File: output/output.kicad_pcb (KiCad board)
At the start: 2 copper layers, 19.1 x 108.5 mm, 60 parts, among them J1 AudioJack2_SwitchT, J2 AudioJack2_SwitchT, J3 Conn_02x05_Odd_Even, J4 AudioJack3, J5 AudioJack3, Q1 MMBT3904, Q2 MMBT3904, U1 NE5532, U2 TL074, U3 NE5532

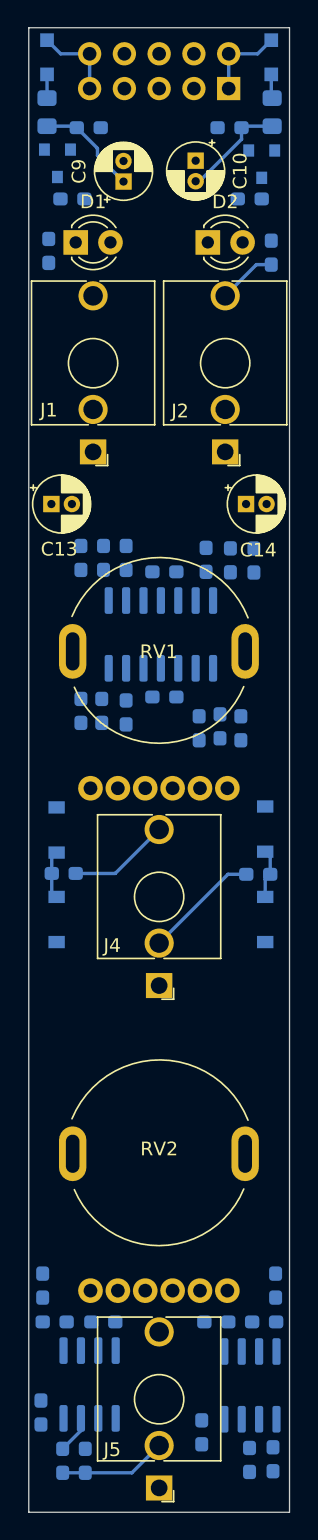
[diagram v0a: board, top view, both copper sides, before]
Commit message: Board layout for Output module
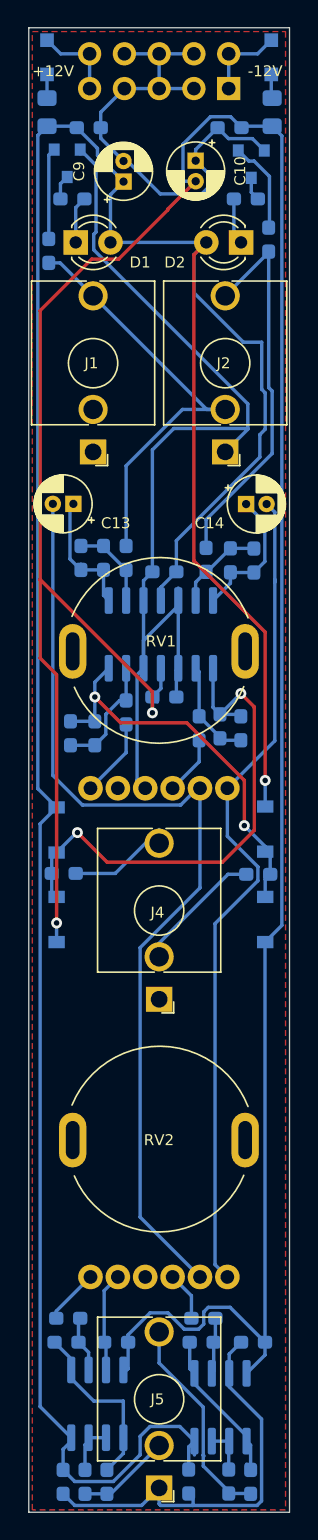
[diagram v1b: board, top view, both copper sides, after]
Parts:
- J1, J2: footprint footprints:Jack_3.5mm_QingPu_WQP-PJ398SM_Vertical_CircularHoles -> kicad_lib:Jack_3.5mm_QingPu_WQP-PJ398SM_Vertical_CircularHoles
- J4, J5: footprint footprints:Jack_3.5mm_QingPu_WQP-WQP419GR_Vertical_CircularHoles -> kicad_lib:Jack_3.5mm_QingPu_WQP-WQP419GR_Vertical_CircularHoles
- RV1, RV2: footprint footprints:Potentiometer_Song_Huei_R1214G_Dual_Vertical -> kicad_lib:Potentiometer_Song_Huei_R1214G_Dual_Vertical
- moved R9 5.79 mm to (202.8, 131.8), turned to 180 degrees
- moved C3 5.32 mm to (192.5, 143.7), turned to 270 degrees
- moved C1 3.72 mm to (201.7, 143.7)
- moved R10 3.03 mm to (192.9, 131.8), turned to 180 degrees
- moved C16 2.81 mm to (193.0, 89.0)
- moved U1 2.71 mm to (204.0, 138.2)
- moved D2 2.43 mm to (205.5, 53.1), turned to 180 degrees
- moved R20 2.32 mm to (206.2, 143.7)
- moved R21 2.24 mm to (194.1, 143.7)
- moved R22 2.20 mm to (195.7, 143.7)
- moved R19 2.19 mm to (204.6, 143.7)
- moved R16 1.93 mm to (194.8, 89.0)
- moved R13 1.83 mm to (202.6, 133.5)
- moved C4 1.75 mm to (196.4, 133.5)
- moved R14 1.72 mm to (192.8, 133.5)
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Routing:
- net +12V: track 7.57 -> 213.4 mm, vias 0 -> 1
- net -12V: track 7.75 -> 199.5 mm, vias 0 -> 2
- net GND: track 0.00 -> 150.7 mm
- net Net-(C13-Pad2): track 0.00 -> 71.3 mm
- net Net-(C14-Pad2): track 0.00 -> 60.9 mm
- net Net-(C15-Pad1): track 3.53 -> 38.2 mm, vias 0 -> 2
- net INL: track 0.00 -> 32.1 mm
- net Net-(C16-Pad1): track 3.61 -> 29.0 mm, vias 0 -> 2
- net INR: track 4.31 -> 28.9 mm
- net Net-(J5-PadT): track 0.00 -> 15.6 mm
- net Net-(R14-Pad1): track 0.00 -> 13.2 mm
- net Net-(R13-Pad1): track 0.00 -> 12.0 mm
- net Net-(C12-Pad1): track 0.00 -> 10.2 mm
- net Net-(C11-Pad1): track 0.00 -> 9.74 mm
- net Net-(C16-Pad2): track 0.00 -> 8.77 mm
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- added copper zone on F.Cu, net GND
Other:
- board text added: "+12V"
- board text added: "-12V"
- board text added: "Output v1.0 www.birchavenue.org"

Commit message: Unhide layers
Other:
- rule pad_to_mask_clearance: 0.05 -> 0
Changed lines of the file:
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@@
   (layers
     (0 F.Cu signal)
-    (31 B.Cu signal hide)
-    (32 B.Adhes user hide)
-    (33 F.Adhes user hide)
-    (34 B.Paste user hide)
-    (35 F.Paste user hide)
+    (31 B.Cu signal)
+    (32 B.Adhes user)
+    (33 F.Adhes user)
+    (34 B.Paste user)
+    (35 F.Paste user)
     (36 B.SilkS user)
     (37 F.SilkS user)
-    (38 B.Mask user hide)
-    (39 F.Mask user hide)
+    (38 B.Mask user)
+    (39 F.Mask user)
     (40 Dwgs.User user)
     (41 Cmts.User user)
@@
     (46 B.CrtYd user)
     (47 F.CrtYd user)
-    (48 B.Fab user hide)
-    (49 F.Fab user hide)
+    (48 B.Fab user)
+    (49 F.Fab user)
   )
   (setup
@@
     (pad_size 1.524 1.524)
     (pad_drill 0.762)
-    (pad_to_mask_clearance 0.05)
+    (pad_to_mask_clearance 0)
     (aux_axis_origin 0 0)
     (visible_elements FFFFFF7F)
@@
       (outputformat 1)
       (mirror false)
-      (drillshape 1)
+      (drillshape 0)
       (scaleselection 1)
-      (outputdirectory ""))
+      (outputdirectory "plots/"))
   )
   (net 0 "")
@@
       (effects (font (size 0.5 0.5) (thickness 0.08)) (justify mirror))
     )
-    (pad 2 smd roundrect (at 1.025 0 90) (size 1.15 1.4) (layers B.Cu B.Paste B.Mask) (roundrect_rratio 0.217391)
+    (pad 2 smd roundrect (at 1.025 0 90) (size 1.15 1.4) (layers B.Cu B.Paste B.Mask) (roundrect_rratio 0.2173904347826087)
       (net 18 "Net-(D4-Pad2)"))
-    (pad 1 smd roundrect (at -1.025 0 90) (size 1.15 1.4) (layers B.Cu B.Paste B.Mask) (roundrect_rratio 0.217391)
+    (pad 1 smd roundrect (at -1.025 0 90) (size 1.15 1.4) (layers B.Cu B.Paste B.Mask) (roundrect_rratio 0.2173904347826087)
       (net 3 -12V))
     (model ${KISYS3DMOD}/Diode_SMD.3dshapes/D_0805_2012Metric.wrl
@@
       (effects (font (size 0.5 0.5) (thickness 0.08)) (justify mirror))
     )
-    (pad 2 smd roundrect (at 1.025 0 90) (size 1.15 1.4) (layers B.Cu B.Paste B.Mask) (roundrect_rratio 0.217391)
+    (pad 2 smd roundrect (at 1.025 0 90) (size 1.15 1.4) (layers B.Cu B.Paste B.Mask) (roundrect_rratio 0.2173904347826087)
       (net 17 "Net-(D3-Pad1)"))
-    (pad 1 smd roundrect (at -1.025 0 90) (size 1.15 1.4) (layers B.Cu B.Paste B.Mask) (roundrect_rratio 0.217391)
+    (pad 1 smd roundrect (at -1.025 0 90) (size 1.15 1.4) (layers B.Cu B.Paste B.Mask) (roundrect_rratio 0.2173904347826087)
       (net 2 +12V))
     (model ${KISYS3DMOD}/Diode_SMD.3dshapes/D_0805_2012Metric.wrl
